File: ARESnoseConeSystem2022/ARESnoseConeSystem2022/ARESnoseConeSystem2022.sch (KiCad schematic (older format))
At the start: 14 parts, among them J1 436500200, J2 436500200, J3 BMP390_Headers, J4 ICM20948_Headers, J5 GPS_Headers1, J6 Transmitter_Headers1, J7 Conn_01x08, J8 Transmitter_Headers2, U1 L7805, U2 Teensy4.1

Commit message: Better regulator
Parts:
- removed U1: L7805, Package_TO_SOT_THT:TO-220-3_Vertical, symbol Regulator_Linear:L7805
- added R2: 3 kOhm, Resistor_SMD:R_0805_2012Metric_Pad1.15x1.40mm_HandSolder, symbol Device:R_US
- added R3: 9,1 kOhm, Resistor_SMD:R_0805_2012Metric_Pad1.15x1.40mm_HandSolder, symbol Device:R_US
- added R4: 10 kOhm, Resistor_SMD:R_0805_2012Metric_Pad1.15x1.40mm_HandSolder, symbol Device:R_US
- added U1: AP2210K-ADJTRG1, SOT-23-5_DIO, symbol 5V-Reg:AP2210K-ADJTRG1
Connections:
- net GND: now also R3.2, R4.2, U1.2 (GND)
- net +BATT: now reaches C2.1, J1.2
- net +BATT: now also J2.2, U1.1 (VIN)
- net at C3.1: now also R2.1, U1.5 (VOUT)
- net at J1.1: now also R4.1, U1.3 (EN); no longer J2.2
- new net: R2.2, R3.1, U1.4 (BYP/ADJ)
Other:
- note added: "VOUT = 1.25V*(1+R3/R2)"
- note removed: "Find a linear reg with enable and disable"
- moved on the sheet: C2, C3, J1, J2

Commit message: Reworked Power & GND
New regulator + ground planes
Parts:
- U1: footprint SOT-23-5_DIO -> footprints:AP2210K-ADJTRG1
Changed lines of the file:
@@
 F 0 "U1" H 3050 1237 60  0000 C CNN
 F 1 "AP2210K-ADJTRG1" H 3050 1131 60  0000 C CNN
-F 2 "SOT-23-5_DIO" H 3050 1090 60  0001 C CNN
+F 2 "footprints:AP2210K-ADJTRG1" H 3050 1090 60  0001 C CNN
 F 3 "" H 2150 850 60  0000 C CNN
 	1    2150 850

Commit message: Gerber files
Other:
- note added: "For questions & comments:\nEric Broman\nerictbroman@gmail.com\n"
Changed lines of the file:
@@
 Connection ~ 1450 850
 Connection ~ 3950 1750
+Text Notes 6550 1000 0    50   ~ 0
+For questions & comments:\nEric Broman\nerictbroman@gmail.com\n
 $EndSCHEMATC

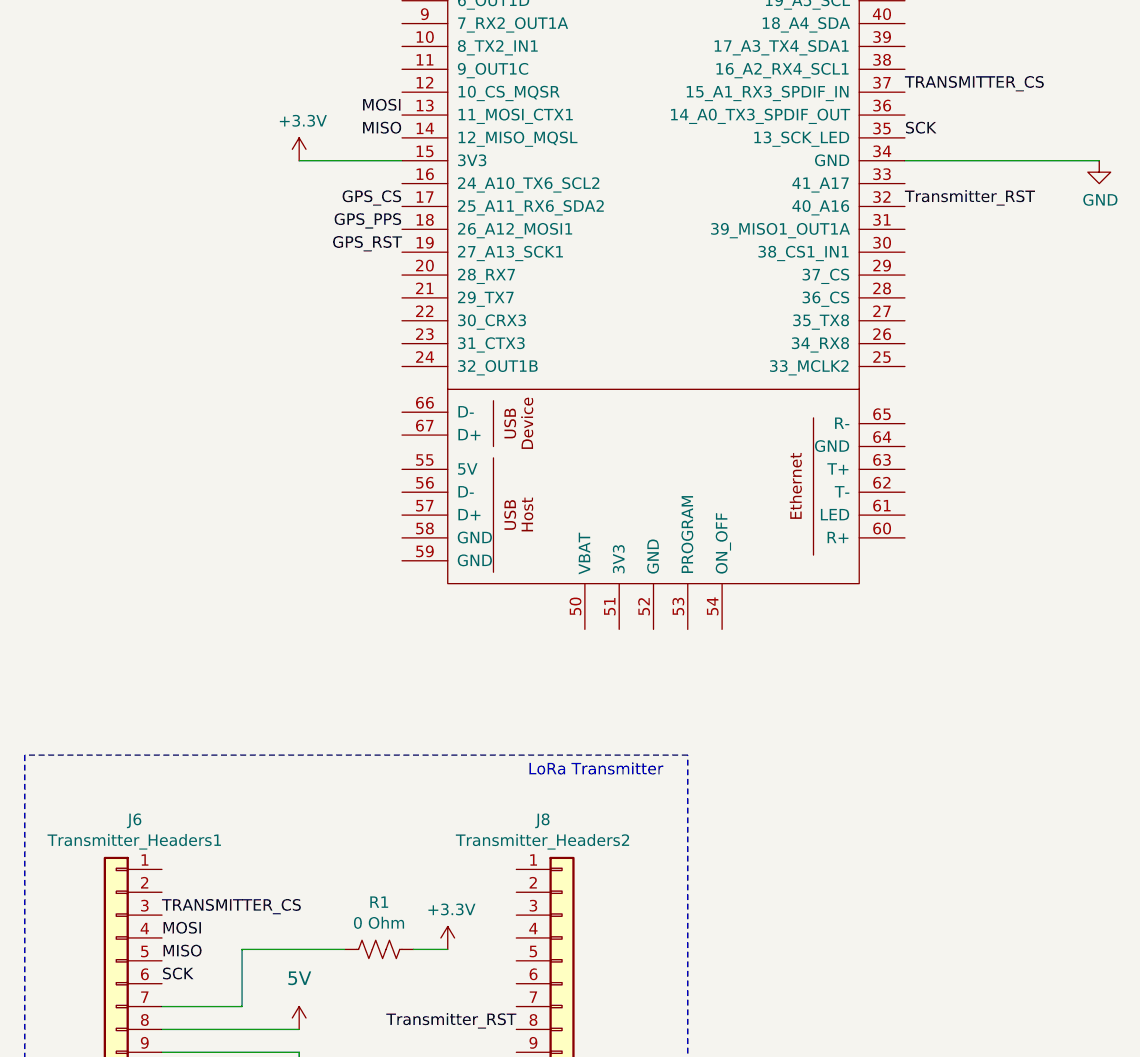
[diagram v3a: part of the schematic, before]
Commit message: Added RXEN & TXEN pins on trasnceiver
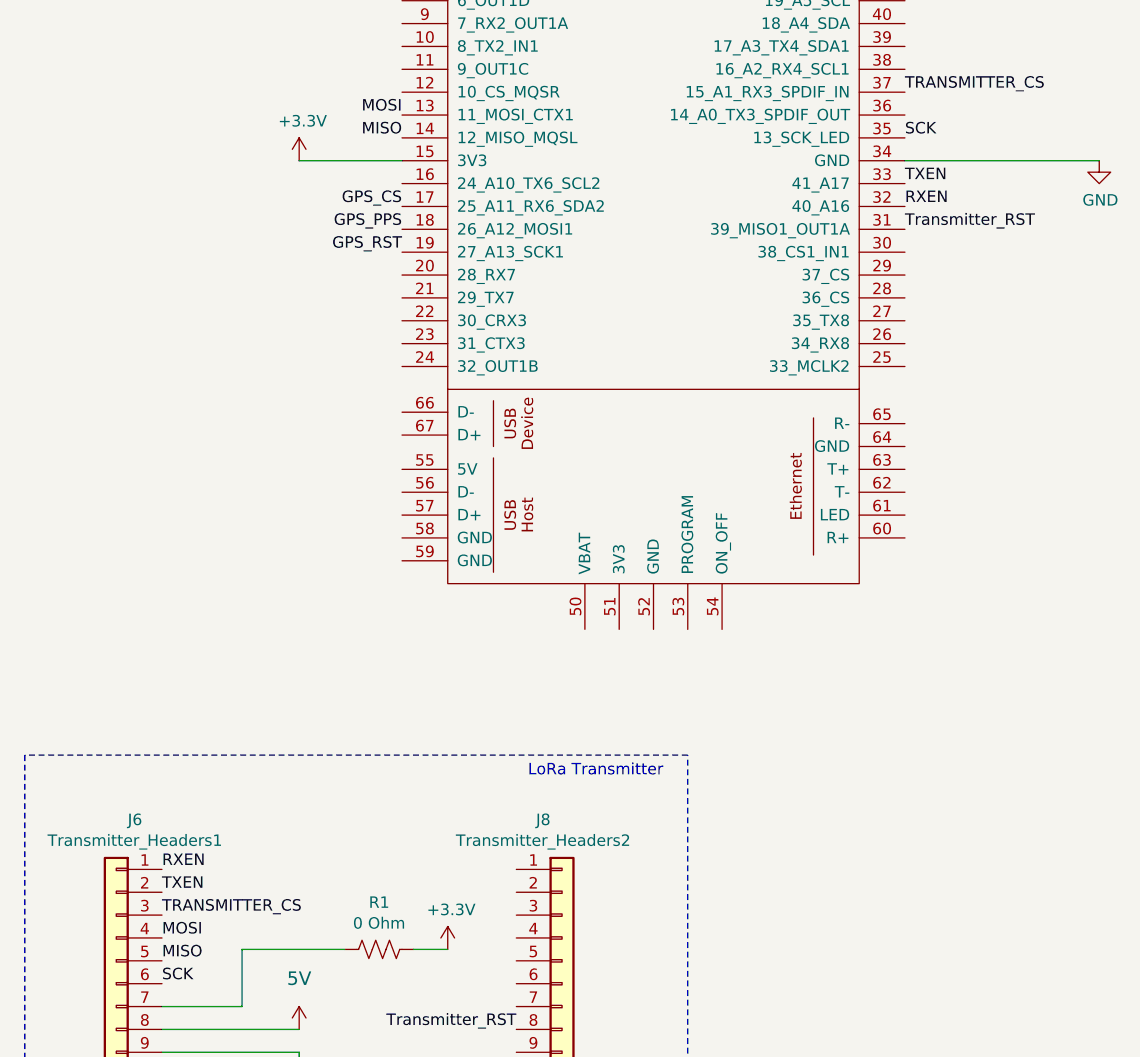
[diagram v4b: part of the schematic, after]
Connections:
- net Transmitter_RST: now also U2.31 (39_MISO1_OUT1A); no longer U2.32 (40_A16)
- net TXEN: now reaches U2.33 (41_A17)
- net TXEN: now also J6.2 (Pin_2)
- net RXEN: now reaches J6.1 (Pin_1)
- net RXEN: now also U2.32 (40_A16)
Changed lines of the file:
@@
 Text Label 6700 7000 2    50   ~ 0
 Transmitter_RST
-Text Label 8400 3400 0    50   ~ 0
+Text Label 8400 3500 0    50   ~ 0
 Transmitter_RST
 Text Label 6200 3500 2    50   ~ 0
@@
 Text Notes 6550 1000 0    50   ~ 0
 For questions & comments:\nEric Broman\nerictbroman@gmail.com\n
+Text Label 8400 3400 0    50   ~ 0
+RXEN
+Text Label 8400 3300 0    50   ~ 0
+TXEN
+Text Label 5150 6300 0    50   ~ 0
+RXEN
+Text Label 5150 6400 0    50   ~ 0
+TXEN
 $EndSCHEMATC

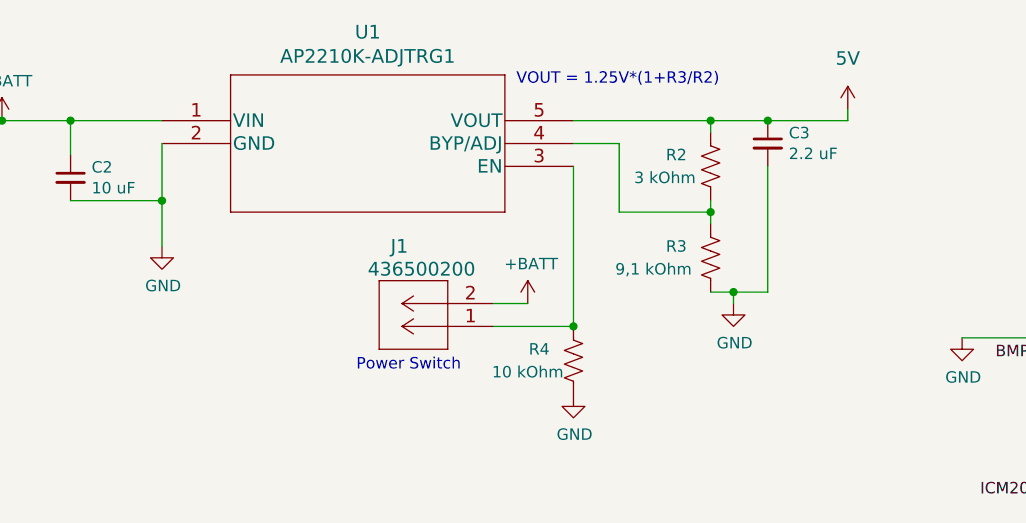
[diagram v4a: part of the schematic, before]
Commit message: Upgrade power
1A LDO instead of 300 mA
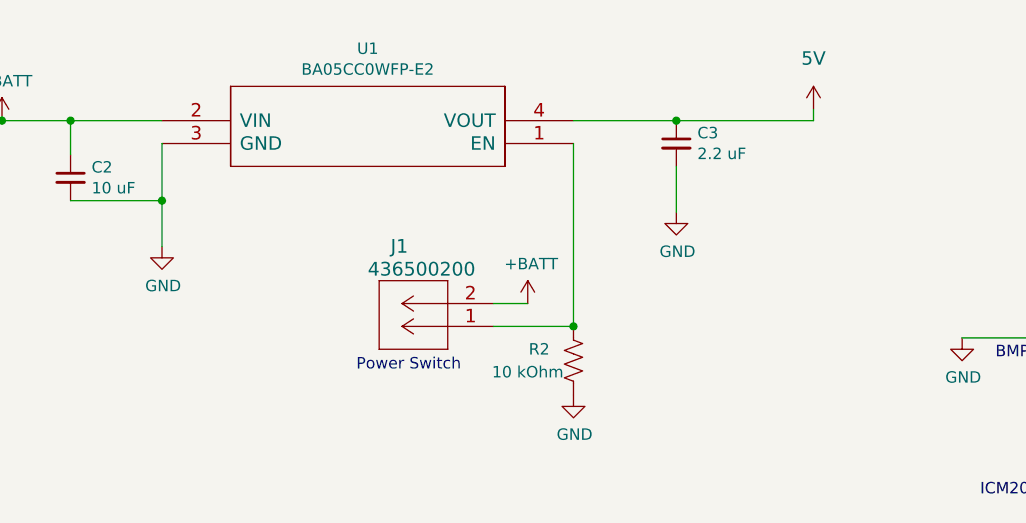
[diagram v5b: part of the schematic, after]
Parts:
- removed R2: 3 kOhm, Resistor_SMD:R_0805_2012Metric_Pad1.15x1.40mm_HandSolder, symbol Device:R_US
- removed R3: 9,1 kOhm, Resistor_SMD:R_0805_2012Metric_Pad1.15x1.40mm_HandSolder, symbol Device:R_US
- removed U1: AP2210K-ADJTRG1, footprints:AP2210K-ADJTRG1, symbol 5V-Reg:AP2210K-ADJTRG1
- added U1: BA05CC0WFP-E2, Package_TO_SOT_SMD:TO-252-5_TabPin3, symbol 5V-Reg:BA05CC0WFP-E2
- renumbered R4 to R2
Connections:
- net +BATT: now also U1.2 (VIN)
- net GND: now also U1.3 (GND)
- net at C3.1: now also U1.4 (VOUT)
- net at J1.1, R2.1: now also U1.1 (EN)
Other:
- note removed: "VOUT = 1.25V*(1+R3/R2)"
- moved on the sheet: C3
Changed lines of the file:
@@
-$EndComp
-$Comp
-L 2021-10-26_01-52-08:436500200 J2
-U 1 1 6179FE90
-P 1100 950
-F 0 "J2" H 1342 563 60  0000 C CNN
-F 1 "436500200" H 1342 669 60  0000 C CNN
-F 2 "Connector_Molex:Molex_Micro-Fit_3.0_43650-0200_1x02_P3.00mm_Horizontal" H 1500 890 60  0001 C CNN
-F 3 "" H 1100 950 60  0000 C CNN
-	1    1100 950
-	-1   0    0    1
 $EndComp
 $Comp
@@
 $EndComp
 $Comp
-L Device:C_Small C3
-U 1 1 617A5197
-P 4800 950
-F 0 "C3" H 4892 996 50  0000 L CNN
-F 1 "2.2 uF" H 4892 905 50  0000 L CNN
-F 2 "Capacitor_SMD:C_0805_2012Metric" H 4800 950 50  0001 C CNN
-F 3 "~" H 4800 950 50  0001 C CNN
-	1    4800 950
-	1    0    0    -1
-$EndComp
-$Comp
 L ARESnoseConeSystem2022-rescue:5V-ARESnoseConeSystem2022-eagle-import #SUPPLY0101
 U 1 1 617A6ADA
-P 5150 800
-F 0 "#SUPPLY0101" H 5150 800 50  0001 C CNN
-F 1 "5V" H 5150 1022 59  0000 C CNN
-F 2 "" H 5150 800 50  0001 C CNN
-F 3 "" H 5150 800 50  0001 C CNN
-	1    5150 800
+P 5000 800
+F 0 "#SUPPLY0101" H 5000 800 50  0001 C CNN
+F 1 "5V" H 5000 1022 59  0000 C CNN
+F 2 "" H 5000 800 50  0001 C CNN
+F 3 "" H 5000 800 50  0001 C CNN
+	1    5000 800
 	1    0    0    -1
 $EndComp
@@
 	-1   0    0    1
 $EndComp
-Text Notes 450  1150 0    50   ~ 0
-Power Input 7.4V LiPo
 Text Notes 3000 1950 0    50   ~ 0
 Power Switch
@@
 F 3 "" H 2150 1400 50  0001 C CNN
 	1    2150 1400
-	1    0    0    -1
-$EndComp
-$Comp
-L power:GND #PWR0102
-U 1 1 6183F6F2
-P 1350 1300
-F 0 "#PWR0102" H 1350 1050 50  0001 C CNN
-F 1 "GND" H 1355 1127 50  0000 C CNN
-F 2 "" H 1350 1300 50  0001 C CNN
-F 3 "" H 1350 1300 50  0001 C CNN
-	1    1350 1300
 	1    0    0    -1
 $EndComp
@@
 Text Notes 4600 7600 0    50   ~ 0
 R1 is to provide 3.3V power.\nMixed instructions if it can be left floating
-$Comp
-L 5V-Reg:AP2210K-ADJTRG1 U1
-U 1 1 6189FD96
-P 2150 850
-F 0 "U1" H 3050 1237 60  0000 C CNN
-F 1 "AP2210K-ADJTRG1" H 3050 1131 60  0000 C CNN
-F 2 "footprints:AP2210K-ADJTRG1" H 3050 1090 60  0001 C CNN
-F 3 "" H 2150 850 60  0000 C CNN
-	1    2150 850
-	1    0    0    -1
-$EndComp
 Wire Wire Line
 	1750 850  1750 1000
@@
 	2150 1200 2150 950
 Connection ~ 2150 1200
-$Comp
-L power:GND #PWR03
-U 1 1 618B8BF2
-P 4650 1650
-F 0 "#PWR03" H 4650 1400 50  0001 C CNN
-F 1 "GND" H 4655 1477 50  0000 C CNN
-F 2 "" H 4650 1650 50  0001 C CNN
-F 3 "" H 4650 1650 50  0001 C CNN
-	1    4650 1650
-	1    0    0    -1
-$EndComp
-Wire Wire Line
-	5150 850  5150 800
+Wire Wire Line
+	5000 850  5000 800
 $Comp
 L power:+BATT #PWR02
@@
 	3600 1650 3750 1650
 Wire Wire Line
-	3950 1050 3950 1750
-Wire Wire Line
 	3950 1750 3600 1750
 $Comp
-L Device:R_US R4
+L Device:R_US R2
 U 1 1 618D4FFE
 P 3950 1900
-F 0 "R4" H 3800 1950 50  0000 C CNN
+F 0 "R2" H 3800 1950 50  0000 C CNN
 F 1 "10 kOhm" H 3750 1850 50  0000 C CNN
 F 2 "Resistor_SMD:R_0805_2012Metric_Pad1.15x1.40mm_HandSolder" V 3990 1890 50  0001 C CNN
@@
 	1    0    0    -1
 $EndComp
-Text Notes 3700 700  0    50   ~ 0
-VOUT = 1.25V*(1+R3/R2)
-Connection ~ 4800 850
-Wire Wire Line
-	4800 850  5150 850
-$Comp
-L Device:R_US R3
-U 1 1 618DF2CA
-P 4550 1450
-F 0 "R3" H 4400 1500 50  0000 C CNN
-F 1 "9,1 kOhm" H 4300 1400 50  0000 C CNN
-F 2 "Resistor_SMD:R_0805_2012Metric_Pad1.15x1.40mm_HandSolder" V 4590 1440 50  0001 C CNN
-F 3 "~" H 4550 1450 50  0001 C CNN
-	1    4550 1450
-	1    0    0    -1
-$EndComp
-$Comp
-L Device:R_US R2
-U 1 1 618E25C7
-P 4550 1050
-F 0 "R2" H 4400 1100 50  0000 C CNN
-F 1 "3 kOhm" H 4350 1000 50  0000 C CNN
-F 2 "Resistor_SMD:R_0805_2012Metric_Pad1.15x1.40mm_HandSolder" V 4590 1040 50  0001 C CNN
-F 3 "~" H 4550 1050 50  0001 C CNN
-	1    4550 1050
-	1    0    0    -1
-$EndComp
-Wire Wire Line
-	3950 850  4550 850
-Wire Wire Line
-	4550 850  4550 900
-Connection ~ 4550 850
-Wire Wire Line
-	4550 850  4800 850
-Wire Wire Line
-	4800 1050 4800 1600
-Wire Wire Line
-	4550 1300 4550 1250
-Wire Wire Line
-	3950 950  4150 950
-Wire Wire Line
-	4150 950  4150 1250
-Wire Wire Line
-	4150 1250 4550 1250
-Connection ~ 4550 1250
-Wire Wire Line
-	4550 1250 4550 1200
-Wire Wire Line
-	4550 1600 4650 1600
-Wire Wire Line
-	4650 1650 4650 1600
-Connection ~ 4650 1600
-Wire Wire Line
-	4650 1600 4800 1600
-Wire Wire Line
-	1100 950  1350 950
-Wire Wire Line
-	1350 950  1350 1300
 Wire Wire Line
 	1100 850  1450 850
@@
 Text Label 5150 6400 0    50   ~ 0
 TXEN
+$Comp
+L 2021-10-26_01-52-08:436500200 J2
+U 1 1 6179FE90
+P 1100 950
+F 0 "J2" H 1342 563 60  0000 C CNN
+F 1 "436500200" H 1342 669 60  0000 C CNN
+F 2 "Connector_Molex:Molex_Micro-Fit_3.0_43650-0200_1x02_P3.00mm_Horizontal" H 1500 890 60  0001 C CNN
+F 3 "" H 1100 950 60  0000 C CNN
+	1    1100 950
+	-1   0    0    1
+$EndComp
+Connection ~ 4400 850
+Wire Wire Line
+	3950 850  4400 850
+Wire Wire Line
+	4400 850  5000 850
+Wire Wire Line
+	4400 1050 4400 1250
+$Comp
+L power:GND #PWR03
+U 1 1 618B8BF2
+P 4400 1250
+F 0 "#PWR03" H 4400 1000 50  0001 C CNN
+F 1 "GND" H 4405 1077 50  0000 C CNN
+F 2 "" H 4400 1250 50  0001 C CNN
+F 3 "" H 4400 1250 50  0001 C CNN
+	1    4400 1250
+	1    0    0    -1
+$EndComp
+$Comp
+L Device:C_Small C3
+U 1 1 617A5197
+P 4400 950
+F 0 "C3" H 4492 996 50  0000 L CNN
+F 1 "2.2 uF" H 4492 905 50  0000 L CNN
+F 2 "Capacitor_SMD:C_0805_2012Metric" H 4400 950 50  0001 C CNN
+F 3 "~" H 4400 950 50  0001 C CNN
+	1    4400 950
+	1    0    0    -1
+$EndComp
+$Comp
+L power:GND #PWR0102
+U 1 1 6183F6F2
+P 1350 1300
+F 0 "#PWR0102" H 1350 1050 50  0001 C CNN
+F 1 "GND" H 1355 1127 50  0000 C CNN
+F 2 "" H 1350 1300 50  0001 C CNN
+F 3 "" H 1350 1300 50  0001 C CNN
+	1    1350 1300
+	1    0    0    -1
+$EndComp
+Wire Wire Line
+	1100 950  1350 950
+Wire Wire Line
+	1350 950  1350 1300
+Text Notes 450  1150 0    50   ~ 0
+Power Input 7.4V LiPo
+$Comp
+L 5V-Reg:BA05CC0WFP-E2 U1
+U 1 1 61D9195C
+P 3100 600
+F 0 "U1" H 3050 665 50  0000 C CNN
+F 1 "BA05CC0WFP-E2" H 3050 574 50  0000 C CNN
+F 2 "Package_TO_SOT_SMD:TO-252-5_TabPin3" H 3100 550 50  0001 C CNN
+F 3 "https://fscdn.rohm.com/en/products/databook/datasheet/ic/power/linear_regulator/baxxdd0-e.pdf" H 3100 550 50  0001 C CNN
+	1    3100 600
+	1    0    0    -1
+$EndComp
+Wire Wire Line
+	3950 950  3950 1750
 $EndSCHEMATC
